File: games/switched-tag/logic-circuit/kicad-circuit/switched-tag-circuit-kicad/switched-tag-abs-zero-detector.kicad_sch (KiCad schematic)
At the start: 19 parts

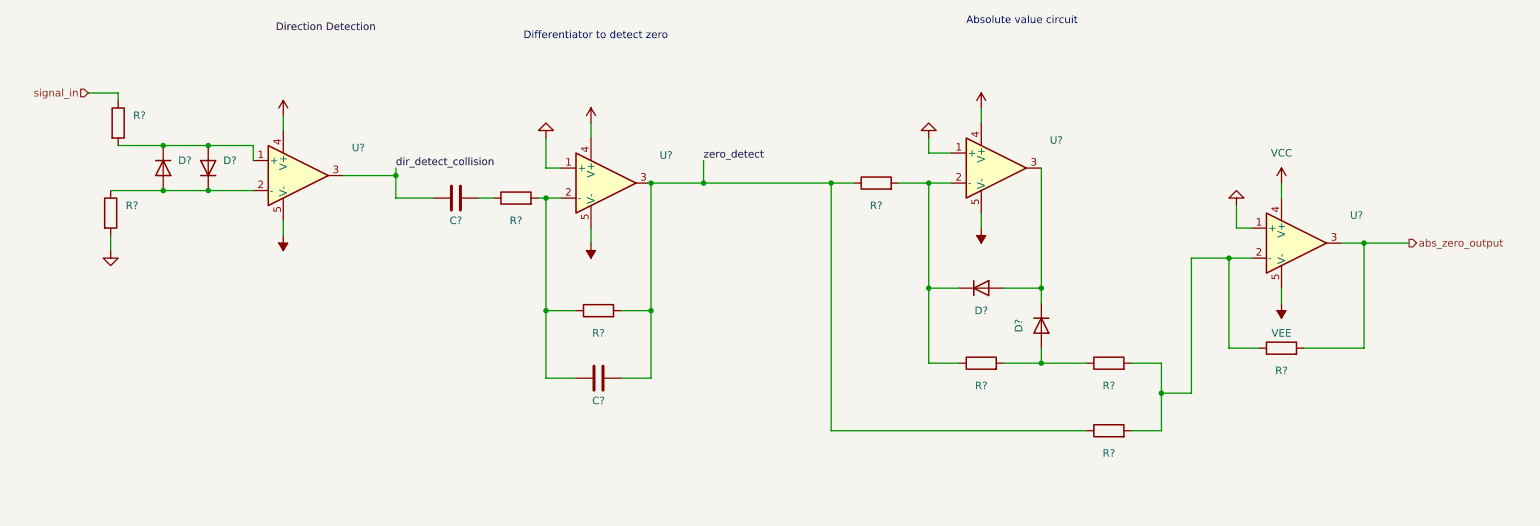
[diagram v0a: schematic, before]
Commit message: Saving progress on kicad schematic. Trying to set up ngspice simulation.
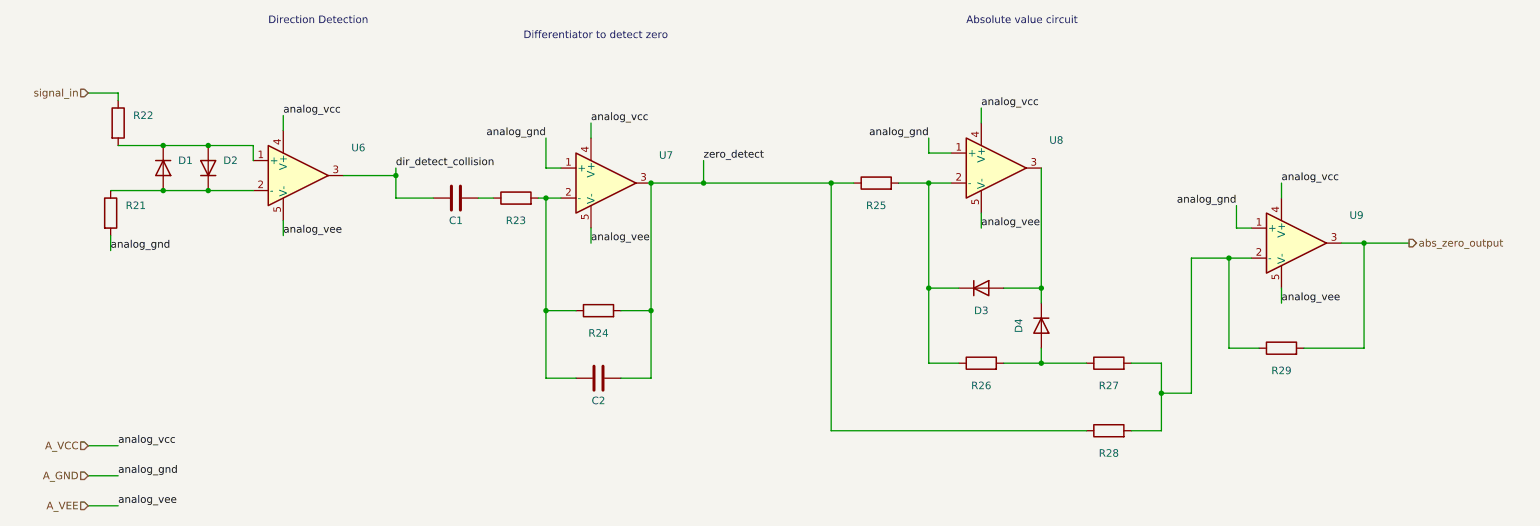
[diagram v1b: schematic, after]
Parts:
- C1, C2: renamed from C?; value ~ -> (none)
- D1, D2, D4: renamed from D?; value ~ -> (none); Spice_Lib_File (none) -> /home/pab/Inventions/analog-circuit-game-console/ms-circuit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
- D3: renamed from D?; value ~ -> (none); Spice_Lib_File (none) -> /home/pab/Inventions/analog-circuit-game-console/ms-circuit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; Spice_Model (none) -> D1N914; Spice_Netlist_Enabled (none) -> Y; Spice_Primitive (none) -> D
- R21, R22, R23, R24, R25, R26, R27, R28, R29: renamed from R?; value ~ -> (none)
- U6, U7, U8, U9: renamed from U?; value ~ -> (none); Spice_Lib_File (none) -> /home/pab/Inventions/analog-circuit-game-console/ms-circuit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; Spice_Model (none) -> LM358; Spice_Node_Sequence (none) -> 1 2 4 5 3
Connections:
- net GND renamed A_GND
- net VCC renamed A_VCC
- net VEE renamed A_VEE
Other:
- note added: "Direction Detection"

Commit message: Fixed problems with kicad circuit adn spice setup.
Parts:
- D1, D2, D4: Spice_Model (none) -> D1N914; Spice_Netlist_Enabled (none) -> Y; Spice_Node_Sequence (none) -> 2 1; Spice_Primitive (none) -> D
- D3: Spice_Node_Sequence (none) -> 2 1
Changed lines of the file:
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@@
+      (effects (font (size 1.27 1.27)) hide)
+    )
+    (property "Spice_Model" "D1N914" (id 5) (at 187.96 125.73 0)
+      (effects (font (size 1.27 1.27)) hide)
+    )
+    (property "Spice_Netlist_Enabled" "Y" (id 6) (at 187.96 125.73 0)
+      (effects (font (size 1.27 1.27)) hide)
+    )
+    (property "Spice_Primitive" "D" (id 7) (at 187.96 125.73 0)
+      (effects (font (size 1.27 1.27)) hide)
+    )
+    (property "Spice_Node_Sequence" "2 1" (id 8) (at 187.96 125.73 0)
       (effects (font (size 1.27 1.27)) hide)
     )
@@
       (effects (font (size 1.27 1.27)) hide)
     )
+    (property "Spice_Model" "D1N914" (id 5) (at 46.99 99.06 0)
+      (effects (font (size 1.27 1.27)) hide)
+    )
+    (property "Spice_Netlist_Enabled" "Y" (id 6) (at 46.99 99.06 0)
+      (effects (font (size 1.27 1.27)) hide)
+    )
+    (property "Spice_Primitive" "D" (id 7) (at 46.99 99.06 0)
+      (effects (font (size 1.27 1.27)) hide)
+    )
+    (property "Spice_Node_Sequence" "2 1" (id 8) (at 46.99 99.06 0)
+      (effects (font (size 1.27 1.27)) hide)
+    )
     (pin "1")
     (pin "2")
@@
       (effects (font (size 1.27 1.27)) hide)
     )
+    (property "Spice_Model" "D1N914" (id 5) (at 39.37 99.06 0)
+      (effects (font (size 1.27 1.27)) hide)
+    )
+    (property "Spice_Netlist_Enabled" "Y" (id 6) (at 39.37 99.06 0)
+      (effects (font (size 1.27 1.27)) hide)
+    )
+    (property "Spice_Primitive" "D" (id 7) (at 39.37 99.06 0)
+      (effects (font (size 1.27 1.27)) hide)
+    )
+    (property "Spice_Node_Sequence" "2 1" (id 8) (at 39.37 99.06 0)
+      (effects (font (size 1.27 1.27)) hide)
+    )
     (pin "1")
     (pin "2")
@@
       (effects (font (size 1.27 1.27)) hide)
     )
+    (property "Spice_Node_Sequence" "2 1" (id 8) (at 177.8 119.38 0)
+      (effects (font (size 1.27 1.27)) hide)
+    )

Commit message: Changed spice model of opamp in kicad sim. Fixed design error in it player determination in ltspice and kicad schematic
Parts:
- U6, U7, U8, U9: Spice_Lib_File /home/pab/Inventions/analog-circuit-game-console/ms-circuit-video-games/spice-models/LM358-onsemi.mod -> /home/pab/Inventions/analog-circuit-game-console/ms-circuit-video-games/spice-models/ada4692.mod; Spice_Model LM358 -> ADA4692
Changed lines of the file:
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@@
       (effects (font (size 1.27 1.27)) (justify left) hide)
     )
-    (property "Spice_Model" "LM358" (id 6) (at 180.34 99.06 0)
-      (effects (font (size 1.27 1.27)) hide)
-    )
-    (property "Spice_Lib_File" "/home/pab/Inventions/analog-circuit-game-console/ms-circuit-video-games/spice-models/LM358-onsemi.mod" (id 7) (at 180.34 99.06 0)
+    (property "Spice_Model" "ADA4692" (id 6) (at 180.34 99.06 0)
+      (effects (font (size 1.27 1.27)) hide)
+    )
+    (property "Spice_Lib_File" "/home/pab/Inventions/analog-circuit-game-console/ms-circuit-video-games/spice-models/ada4692.mod" (id 7) (at 180.34 99.06 0)
       (effects (font (size 1.27 1.27)) hide)
     )
@@
       (effects (font (size 1.27 1.27)) (justify left) hide)
     )
-    (property "Spice_Model" "LM358" (id 6) (at 114.3 101.6 0)
-      (effects (font (size 1.27 1.27)) hide)
-    )
-    (property "Spice_Lib_File" "/home/pab/Inventions/analog-circuit-game-console/ms-circuit-video-games/spice-models/LM358-onsemi.mod" (id 7) (at 114.3 101.6 0)
+    (property "Spice_Model" "ADA4692" (id 6) (at 114.3 101.6 0)
+      (effects (font (size 1.27 1.27)) hide)
+    )
+    (property "Spice_Lib_File" "/home/pab/Inventions/analog-circuit-game-console/ms-circuit-video-games/spice-models/ada4692.mod" (id 7) (at 114.3 101.6 0)
       (effects (font (size 1.27 1.27)) hide)
     )
@@
       (effects (font (size 1.27 1.27)) (justify left) hide)
     )
-    (property "Spice_Model" "LM358" (id 6) (at 62.23 100.33 0)
-      (effects (font (size 1.27 1.27)) hide)
-    )
-    (property "Spice_Lib_File" "/home/pab/Inventions/analog-circuit-game-console/ms-circuit-video-games/spice-models/LM358-onsemi.mod" (id 7) (at 62.23 100.33 0)
+    (property "Spice_Model" "ADA4692" (id 6) (at 62.23 100.33 0)
+      (effects (font (size 1.27 1.27)) hide)
+    )
+    (property "Spice_Lib_File" "/home/pab/Inventions/analog-circuit-game-console/ms-circuit-video-games/spice-models/ada4692.mod" (id 7) (at 62.23 100.33 0)
       (effects (font (size 1.27 1.27)) hide)
     )
@@
       (effects (font (size 1.27 1.27)) (justify left) hide)
     )
-    (property "Spice_Model" "LM358" (id 6) (at 231.14 111.76 0)
-      (effects (font (size 1.27 1.27)) hide)
-    )
-    (property "Spice_Lib_File" "/home/pab/Inventions/analog-circuit-game-console/ms-circuit-video-games/spice-models/LM358-onsemi.mod" (id 7) (at 231.14 111.76 0)
-      (effects (font (size 1.27 1.27)) hide)
-    )
+    (property "Spice_Model" "ADA4692" (id 6) (at 231.14 111.76 0)
+      (effects (font (size 1.27 1.27)) hide)
+    )
+    (property "Spice_Lib_File" "/home/pab/Inventions/analog-circuit-game-console/ms-circuit-video-games/spice-models/ada4692.mod" (id 7) (at 231.14 111.76 0)
+      (effects (font (size 1.27 1.27)) hide)
+    )

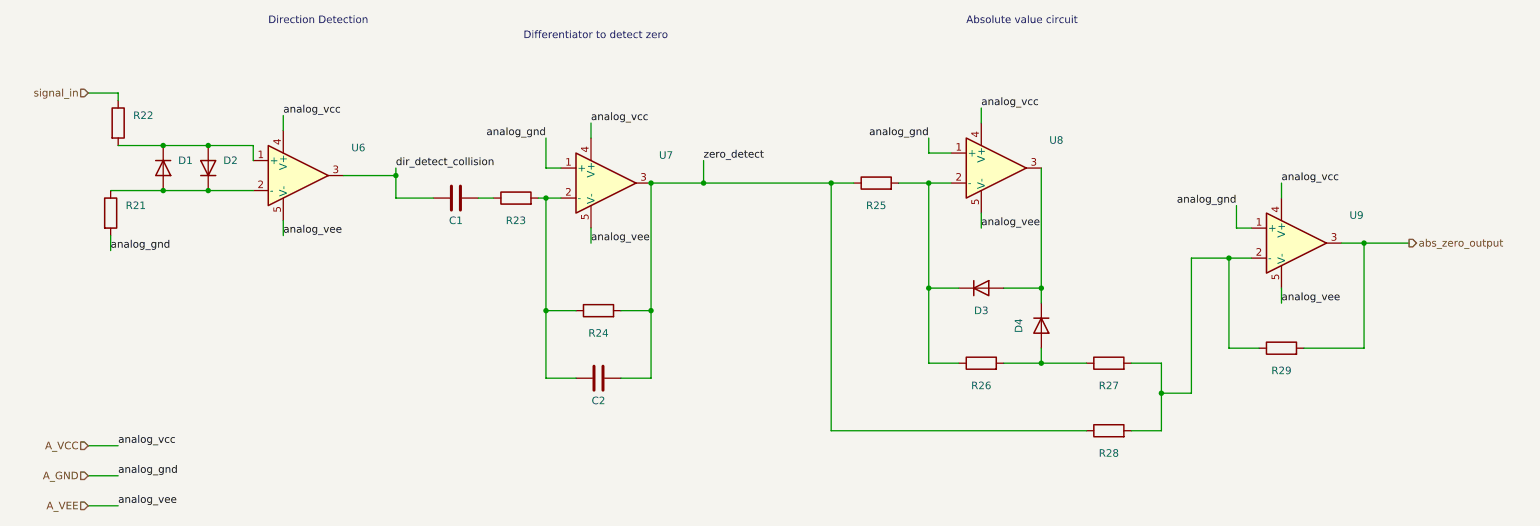
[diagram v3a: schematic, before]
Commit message: Updated kicad circuit. The kicad sim and ltspice do not match up well. Need to fix.
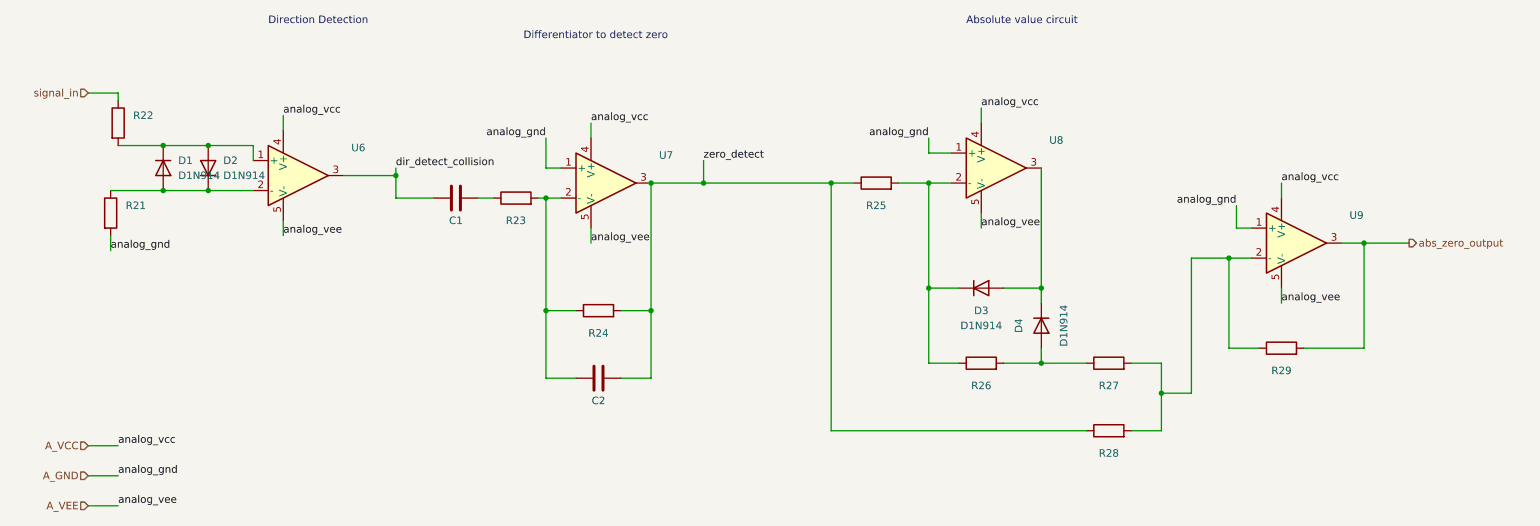
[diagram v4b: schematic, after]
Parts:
- D1, D2, D3, D4: value (none) -> D1N914
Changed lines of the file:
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@@
     (in_bom yes) (on_board yes)
     (property "Reference" "D4" (id 0) (at 184.15 125.73 0))
-    (property "Value" "" (id 1) (at 191.77 125.73 0))
+    (property "Value" "D1N914" (id 1) (at 191.77 125.73 0))
     (property "Footprint" "" (id 2) (at 187.96 125.73 0)
       (effects (font (size 1.27 1.27)) hide)
@@
       (effects (font (size 1.27 1.27)) (justify right))
     )
-    (property "Value" "" (id 1) (at 49.53 100.3299 90)
+    (property "Value" "D1N914" (id 1) (at 49.53 100.3299 90)
       (effects (font (size 1.27 1.27)) (justify right))
     )
@@
       (effects (font (size 1.27 1.27)) hide)
     )
-    (property "Datasheet" "~" (id 3) (at 46.99 99.06 0)
+    (property "Datasheet" "1n914" (id 3) (at 46.99 99.06 0)
       (effects (font (size 1.27 1.27)) hide)
     )
@@
       (effects (font (size 1.27 1.27)) (justify left))
     )
-    (property "Value" "" (id 1) (at 41.91 100.3299 90)
+    (property "Value" "D1N914" (id 1) (at 41.91 100.3299 90)
       (effects (font (size 1.27 1.27)) (justify left))
     )
@@
     (in_bom yes) (on_board yes)
     (property "Reference" "D3" (id 0) (at 177.8 123.19 0))
-    (property "Value" "" (id 1) (at 177.8 125.73 0))
+    (property "Value" "D1N914" (id 1) (at 177.8 125.73 0))
     (property "Footprint" "" (id 2) (at 177.8 119.38 0)
       (effects (font (size 1.27 1.27)) hide)

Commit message: Added some prep work for console hardware.
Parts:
- D1, D2, D3, D4: value D1N914 -> (none); Spice_Lib_File /home/pab/Inventions/analog-circuit-game-console/ms-circuit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 -> ../../../../../spice-models/1N914.lib
- U6, U7, U8, U9: Spice_Lib_File /home/pab/Inventions/analog-circuit-game-console/ms-circuit-video-games/spice-models/ada4692.mod -> /home/pab/Inventions/analog-circuit-game-console/ms-circuit-video-games/spice-models/lmx58_lm2904.lib; Spice_Model ADA4692 -> LMX58_LM2904
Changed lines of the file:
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@@
     (in_bom yes) (on_board yes)
     (property "Reference" "D4" (id 0) (at 184.15 125.73 0))
-    (property "Value" "D1N914" (id 1) (at 191.77 125.73 0))
+    (property "Value" "" (id 1) (at 191.77 125.73 0))
     (property "Footprint" "" (id 2) (at 187.96 125.73 0)
       (effects (font (size 1.27 1.27)) hide)
@@
       (effects (font (size 1.27 1.27)) hide)
     )
-    (property "Spice_Lib_File" "/home/pab/Inventions/analog-circuit-game-console/ms-circuit-video-games/spice-models/1N914.lib" (id 4) (at 187.96 125.73 0)
+    (property "Spice_Lib_File" "../../../../../spice-models/1N914.lib" (id 4) (at 187.96 125.73 0)
       (effects (font (size 1.27 1.27)) hide)
     )
@@
       (effects (font (size 1.27 1.27)) (justify left) hide)
     )
-    (property "Spice_Model" "ADA4692" (id 6) (at 180.34 99.06 0)
-      (effects (font (size 1.27 1.27)) hide)
-    )
-    (property "Spice_Lib_File" "/home/pab/Inventions/analog-circuit-game-console/ms-circuit-video-games/spice-models/ada4692.mod" (id 7) (at 180.34 99.06 0)
+    (property "Spice_Model" "LMX58_LM2904" (id 6) (at 180.34 99.06 0)
+      (effects (font (size 1.27 1.27)) hide)
+    )
+    (property "Spice_Lib_File" "/home/pab/Inventions/analog-circuit-game-console/ms-circuit-video-games/spice-models/lmx58_lm2904.lib" (id 7) (at 180.34 99.06 0)
       (effects (font (size 1.27 1.27)) hide)
     )
@@
       (effects (font (size 1.27 1.27)) (justify left) hide)
     )
-    (property "Spice_Model" "ADA4692" (id 6) (at 114.3 101.6 0)
-      (effects (font (size 1.27 1.27)) hide)
-    )
-    (property "Spice_Lib_File" "/home/pab/Inventions/analog-circuit-game-console/ms-circuit-video-games/spice-models/ada4692.mod" (id 7) (at 114.3 101.6 0)
+    (property "Spice_Model" "LMX58_LM2904" (id 6) (at 114.3 101.6 0)
+      (effects (font (size 1.27 1.27)) hide)
+    )
+    (property "Spice_Lib_File" "/home/pab/Inventions/analog-circuit-game-console/ms-circuit-video-games/spice-models/lmx58_lm2904.lib" (id 7) (at 114.3 101.6 0)
       (effects (font (size 1.27 1.27)) hide)
     )
@@
       (effects (font (size 1.27 1.27)) (justify left) hide)
     )
-    (property "Spice_Model" "ADA4692" (id 6) (at 62.23 100.33 0)
-      (effects (font (size 1.27 1.27)) hide)
-    )
-    (property "Spice_Lib_File" "/home/pab/Inventions/analog-circuit-game-console/ms-circuit-video-games/spice-models/ada4692.mod" (id 7) (at 62.23 100.33 0)
+    (property "Spice_Model" "LMX58_LM2904" (id 6) (at 62.23 100.33 0)
+      (effects (font (size 1.27 1.27)) hide)
+    )
+    (property "Spice_Lib_File" "/home/pab/Inventions/analog-circuit-game-console/ms-circuit-video-games/spice-models/lmx58_lm2904.lib" (id 7) (at 62.23 100.33 0)
       (effects (font (size 1.27 1.27)) hide)
     )
@@
       (effects (font (size 1.27 1.27)) (justify right))
     )
-    (property "Value" "D1N914" (id 1) (at 49.53 100.3299 90)
+    (property "Value" "" (id 1) (at 49.53 100.3299 90)
       (effects (font (size 1.27 1.27)) (justify right))
     )
@@
       (effects (font (size 1.27 1.27)) hide)
     )
-    (property "Spice_Lib_File" "/home/pab/Inventions/analog-circuit-game-console/ms-circuit-video-games/spice-models/1N914.lib" (id 4) (at 46.99 99.06 0)
+    (property "Spice_Lib_File" "../../../../../spice-models/1N914.lib" (id 4) (at 46.99 99.06 0)
       (effects (font (size 1.27 1.27)) hide)
     )
@@
       (effects (font (size 1.27 1.27)) (justify left))
     )
-    (property "Value" "D1N914" (id 1) (at 41.91 100.3299 90)
+    (property "Value" "" (id 1) (at 41.91 100.3299 90)
       (effects (font (size 1.27 1.27)) (justify left))
     )
@@
       (effects (font (size 1.27 1.27)) hide)
     )
-    (property "Spice_Lib_File" "/home/pab/Inventions/analog-circuit-game-console/ms-circuit-video-games/spice-models/1N914.lib" (id 4) (at 39.37 99.06 0)
+    (property "Spice_Lib_File" "../../../../../spice-models/1N914.lib" (id 4) (at 39.37 99.06 0)
       (effects (font (size 1.27 1.27)) hide)
     )
@@
     (in_bom yes) (on_board yes)
     (property "Reference" "D3" (id 0) (at 177.8 123.19 0))
-    (property "Value" "D1N914" (id 1) (at 177.8 125.73 0))
+    (property "Value" "" (id 1) (at 177.8 125.73 0))
     (property "Footprint" "" (id 2) (at 177.8 119.38 0)
       (effects (font (size 1.27 1.27)) hide)
@@
       (effects (font (size 1.27 1.27)) hide)
     )
-    (property "Spice_Lib_File" "/home/pab/Inventions/analog-circuit-game-console/ms-circuit-video-games/spice-models/1N914.lib" (id 7) (at 177.8 119.38 0)
+    (property "Spice_Lib_File" "../../../../../spice-models/1N914.lib" (id 7) (at 177.8 119.38 0)
       (effects (font (size 1.27 1.27)) hide)
     )
@@
       (effects (font (size 1.27 1.27)) (justify left) hide)
     )
-    (property "Spice_Model" "ADA4692" (id 6) (at 231.14 111.76 0)
-      (effects (font (size 1.27 1.27)) hide)
-    )
-    (property "Spice_Lib_File" "/home/pab/Inventions/analog-circuit-game-console/ms-circuit-video-games/spice-models/ada4692.mod" (id 7) (at 231.14 111.76 0)
-      (effects (font (size 1.27 1.27)) hide)
-    )
+    (property "Spice_Model" "LMX58_LM2904" (id 6) (at 231.14 111.76 0)
+      (effects (font (size 1.27 1.27)) hide)
+    )
+    (property "Spice_Lib_File" "/home/pab/Inventions/analog-circuit-game-console/ms-circuit-video-games/spice-models/lmx58_lm2904.lib" (id 7) (at 231.14 111.76 0)
+      (effects (font (size 1.27 1.27)) hide)
+    )
